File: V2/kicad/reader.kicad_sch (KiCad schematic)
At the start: 61 parts, among them U1 MLD-TF PUSH-H18, U2 MAX98357AETE+T, U3 MCP16301Hx-xCH, U4 TCAN1057AVDRQ1, U6 STM32H523CET6, Y1 16MHz

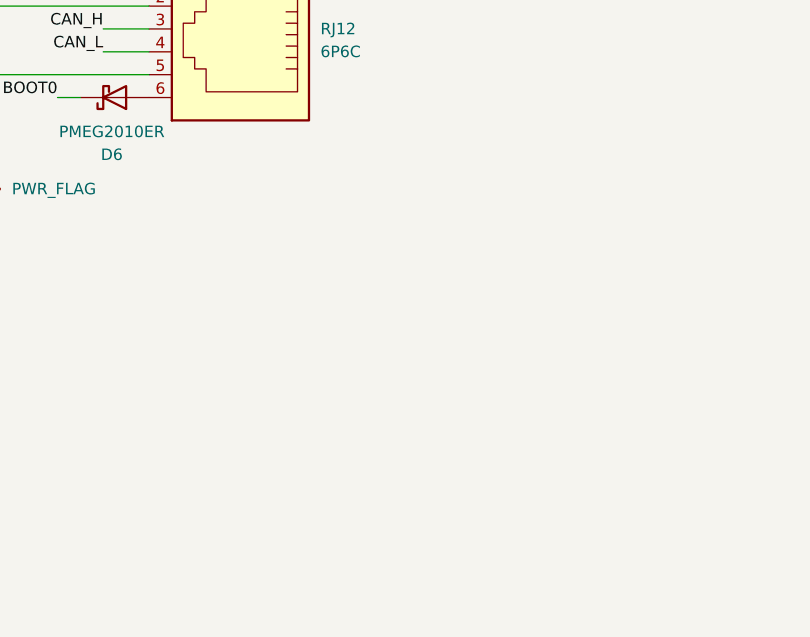
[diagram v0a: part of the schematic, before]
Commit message: added .gitatributes to force LF files. added ethernet connecotr , not yet connected
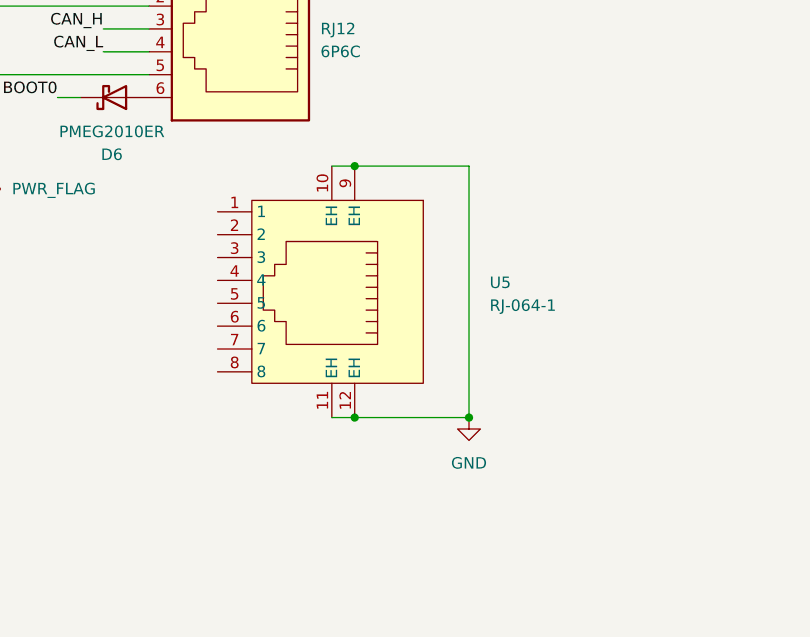
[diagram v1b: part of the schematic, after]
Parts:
- added U5: RJ-064-1, easyeda2kicad:CONN-SMD_RJ-064, symbol easyeda2kicad:RJ-064-1
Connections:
- net GND: now also U5.10 (EH), U5.11 (EH), U5.12 (EH), U5.9 (EH)

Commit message: connected ethernet cable. counting with CAT5 configuration
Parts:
- removed D6: PMEG2010ER, Diode_SMD:Nexperia_CFP3_SOD-123W, symbol Device:D_Schottky
- removed RJ12: 6P6C, Connector_RJ:RJ12_Amphenol_54601-x06_Horizontal, symbol Connector:6P6C
- added D10, D7, D8, D9: PMEG2010ER, Diode_SMD:Nexperia_CFP3_SOD-123W, symbol Device:D_Schottky
- added R14, R17: RC0402FR-07120RL, easyeda2kicad:R0402, symbol easyeda2kicad:RC0402FR-07120RL
- added R15, R16: 10 K, Resistor_SMD:R_0603_1608Metric, symbol Device:R
- added R18: RC0402JR-071KL, easyeda2kicad:R0402, symbol easyeda2kicad:RC0402JR-071KL
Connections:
- net +3.3V: now also R15.1
- net +5V: now also D7.1 (K)
- net BOOT0: now also U5.3, R16.1, R18.2
- net CAN_H: now also U5.4, R14.2
- net CAN_L: now also U5.5, R14.1
- net GND: now also U5.2, U5.7, R16.2
- net NRST: now also U5.6, R15.2, R17.2
- net at U5.1: now also D5.2 (A)
- net at U5.8: now also D7.2 (A)
- new net: D9.1 (K), R17.1
- new net: D10.1 (K), R18.1
- new net BOOT0_ETH: D10.2 (A)
- new net NRST_ETH: D9.2 (A)
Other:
- note added: "TIA/EIA-568-B.1-2001 T568B Wiring"
- moved on the sheet: C16, C28, C29, C30, C31, C32, C33, C34, C35, FB2, RESET1, U5

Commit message: cleaning and pin change in progress
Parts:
- removed D5, D8: PMEG2010ER, Diode_SMD:Nexperia_CFP3_SOD-123W, symbol Device:D_Schottky
- added R19, R20: 10 K, Resistor_SMD:R_0603_1608Metric, symbol Device:R
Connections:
- net BOOT0_ETH is gone; now on net BOOT0: D10.2 (A)
- net NRST_ETH is gone; now on an unnamed net: D9.2 (A)
- net SDMMC_CK is gone; now on net SD_SCK: U1.5 (CLX)
- net +3.3V: now also R19.1, R20.1
- net BOOT0: no longer R16.1, R18.2, U6.44 (BOOT0)
- net FDCAN_RX: now also U6.45 (PB8)
- net FDCAN_TX: now also U6.43 (PB7)
- net I2S_BCLK: no longer U6.19 (PB1)
- net I2S_DATA: no longer U6.18 (PB0)
- net I2S_LRCLK: no longer U6.20 (PB2)
- net LED_G1: no longer U6.17 (PA7)
- net LED_G2: no longer U6.30 (PA9)
- net LED_R1: no longer U6.16 (PA6)
- net LED_R2: no longer U6.29 (PA8)
- net NRST: now also D9.1 (K); no longer C16.1, R15.2, R17.2, RESET1.1, U6.7 (NRST)
- net RFID_IRQ: no longer U6.40 (PB4)
- net RFID_MISO: no longer U6.43 (PB7)
- net RFID_MOSI: no longer U6.45 (PB8)
- net RFID_RST: no longer U6.10 (PA0)
- net RFID_SCK: no longer U6.42 (PB6)
- net RFID_SDA: no longer U6.41 (PB5)
- net SD_DETECTED: now also U6.19 (PB1)
- net SWCLK: now also U6.37 (PA14); no longer U6.28 (PB15)
- net SWDIO: now also U6.34 (PA13); no longer U6.27 (PB14)
- net TRACESWO: now also U6.38 (PA15); no longer U6.13 (PA3)
- net USB_D+: now also U6.32 (PA11); no longer U6.26 (PB13)
- net USB_D-: now also U6.33 (PA12); no longer U6.25 (PB12)
- net at R17.1: no longer D9.1 (K)
- net at U5.1: now also D7.2 (A), U5.8
- net SD_SCK: now reaches U6.15 (PA5)
- net +3.3VA: no longer names the net of C33.1, C34.1, FB2.1, U6.9 (VDDA)
- net GAIN_SLOT: no longer names the net of R1.1, R2.1, U2.2 (GAIN_SLOT)
- net HSE_IN: no longer names the net of C4.1, U6.5 (PH0-OSC_IN), Y1.3
- net HSE_OUT: no longer names the net of C1.1, U6.6 (PH1-OSC_OUT), Y1.1
- net SDMMC_CMD renamed SD_MOSI
- net SD_MOSI: now also U6.17 (PA7)
- net SDMMC_D0 renamed SD_MISO
- net SD_MISO: now also U6.16 (PA6)
- net SDMMC_D1: no longer names the net of U1.8 (DAT1)
- net SDMMC_D1: now also R20.2
- net SDMMC_D2: no longer names the net of U1.1 (DAT2)
- net SDMMC_D2: now also R19.2
- net SDMMC_D3 renamed SD_CS
- net SD_CS: now also U6.18 (PB0)
- new net: C16.1, R15.2, R17.2, RESET1.1, U6.7 (NRST)
- new net: R16.1, R18.2, U6.44 (BOOT0)
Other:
- note added: "cap protects against parasitic resets and bounces."
- note removed: "NRST cap protects against parasitic resets and bounces."
- moved on the sheet: C1, C16, C28, C29, C30, C31, C32, C33, C34, C35, C36, C4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

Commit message: cleaned scheamtic. wired correct pins of mcu... their selection is  in the stm32 selector
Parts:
- removed R17: RC0402FR-07120RL, easyeda2kicad:R0402, symbol easyeda2kicad:RC0402FR-07120RL
- removed R18: RC0402JR-071KL, easyeda2kicad:R0402, symbol easyeda2kicad:RC0402JR-071KL
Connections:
- net I2S_LRCLK is gone; now on net I2S_WS: U2.14 (LRCLK)
- net +3.3V: no longer U6.1 (VBAT)
- net BOOT0: no longer BOOT1.2 (B)
- net I2S_BCLK: now also U6.39 (PB3)
- net I2S_DATA: now also U6.13 (PA3)
- net LED_G1: now also U6.12 (PA2)
- net LED_G2: now also U6.42 (PB6)
- net LED_R1: now also U6.11 (PA1)
- net LED_R2: now also U6.41 (PB5)
- net RFID_IRQ: now also U6.21 (PB10)
- net RFID_MISO: now also U6.27 (PB14)
- net RFID_MOSI: now also U6.28 (PB15)
- net RFID_RST: now also U6.25 (PB12)
- net RFID_SCK: now also U6.20 (PB2)
- net RFID_SDA: now also U6.26 (PB13)
- net at C16.1, R15.2, RESET1.1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: now also D9.2 (A)
- net at D10.1 (K): now also BOOT1.2 (B), R16.1, U6.44 (BOOT0)
- net I2S_WS: now reaches U6.14 (PA4)
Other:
- moved on the sheet: BOOT1, C1, C12, C14, C15, C16, C17, C23, C28, C29, C30, C31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

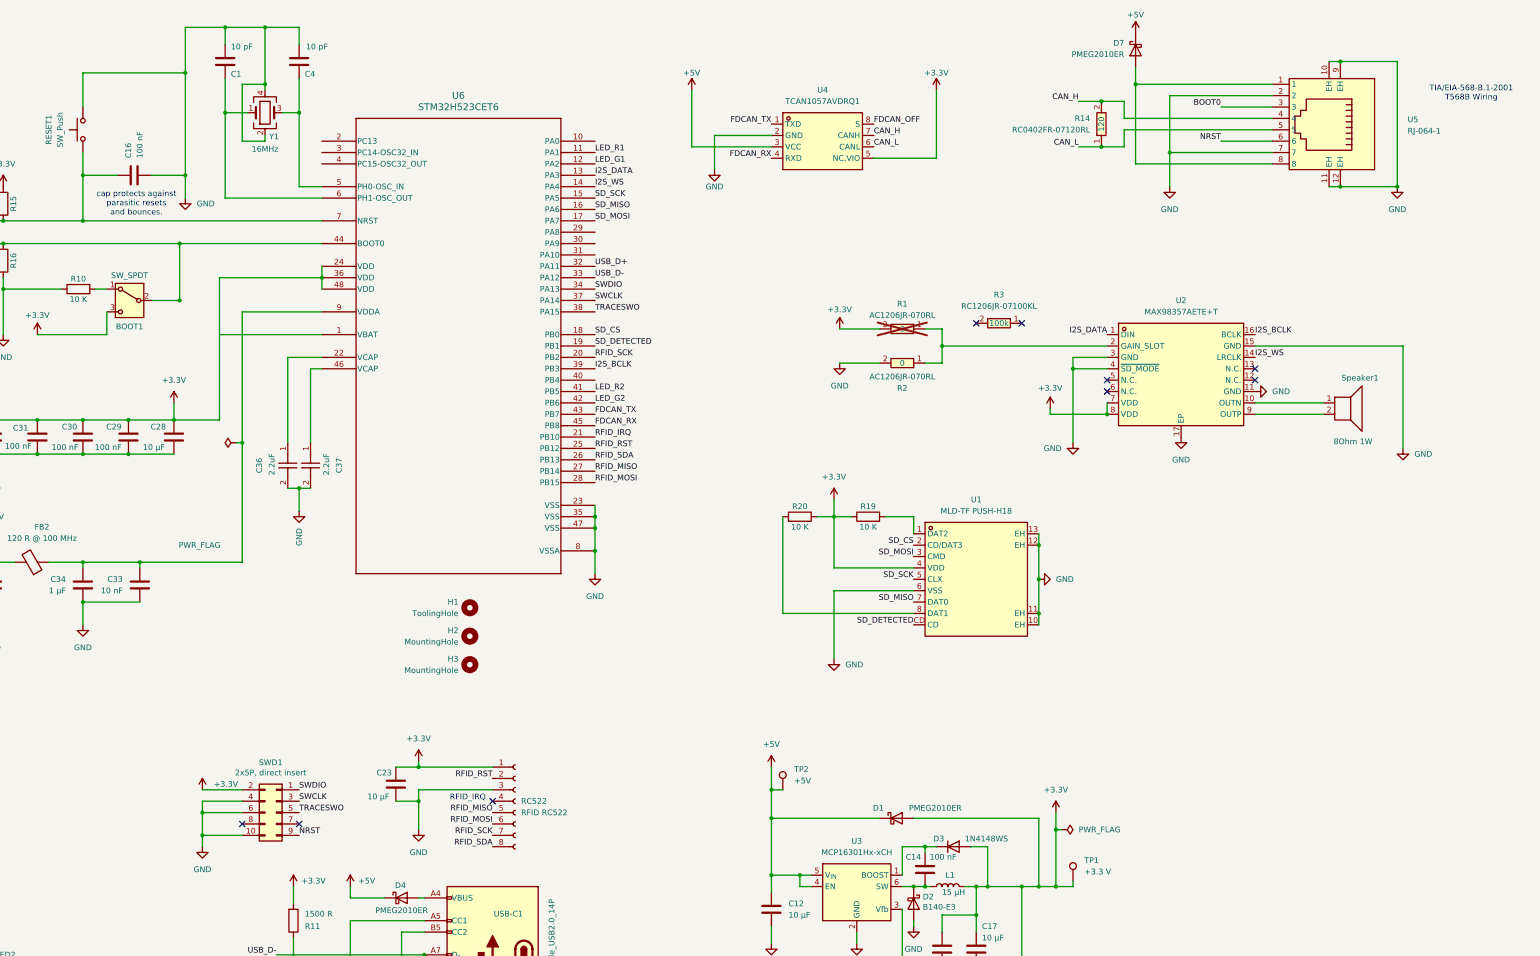
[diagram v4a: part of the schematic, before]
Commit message: Cleaned schematic and removed RFID_IRQ pin
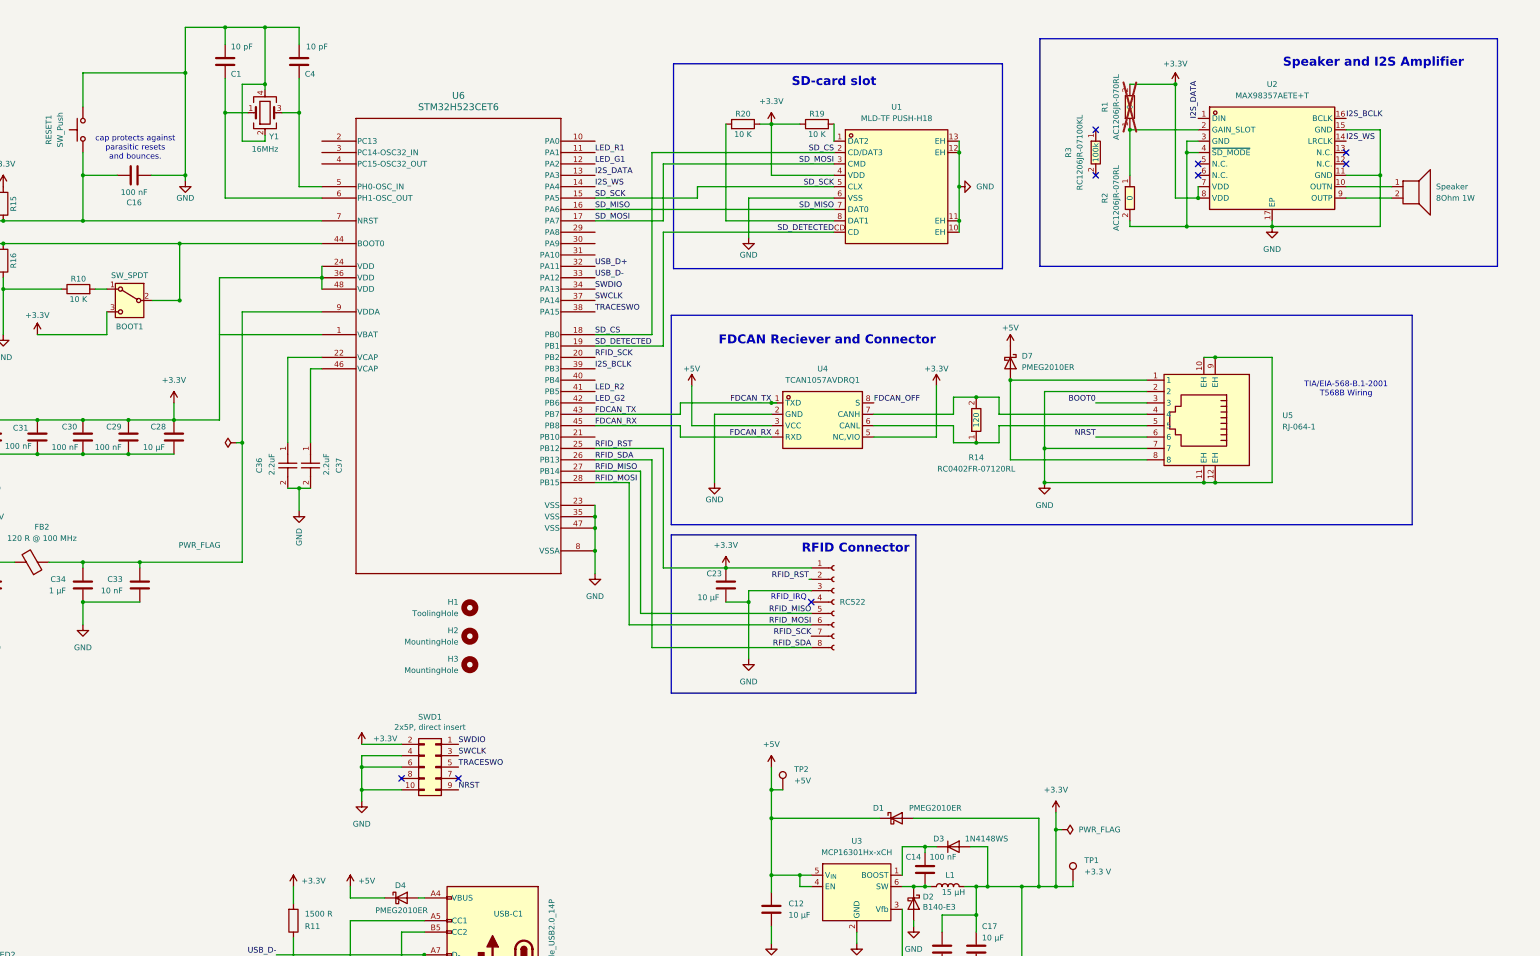
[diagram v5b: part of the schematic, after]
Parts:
- renumbered Speaker1 to Speaker
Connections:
- net RFID_RST is gone; now on net +3.3V: RC522.2 (Pin_2), U6.25 (PB12)
- net RFID_IRQ: no longer U6.21 (PB10)
- net CAN_H: no longer names the net of R14.2, U4.7 (CANH), U5.4
- net CAN_L: no longer names the net of R14.1, U4.6 (CANL), U5.5
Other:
- note added: "FDCAN Reciever and Connector"
- note added: "RFID Connector"
- note added: "SD-card slot"
- note added: "Speaker and I2S Amplifier"
- moved on the sheet: D7, R1, R14, R19, R2, R3, RC522, SWD1, Speaker, U1, U2, U4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

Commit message: small schema changes
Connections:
- net +3.3V: now also R19.2; no longer R19.1
- net at U1.1 (DAT2): now also R19.1; no longer R19.2
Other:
- moved on the sheet: R19, R20, TP4, TP5
